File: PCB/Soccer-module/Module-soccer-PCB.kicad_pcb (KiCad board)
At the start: 2 copper layers, 60 x 60 mm, 6 parts, among them J2 Conn_01x06, J4 Conn_01x02, J5 Conn_01x02, J6 Conn_01x02, U1 TB6612

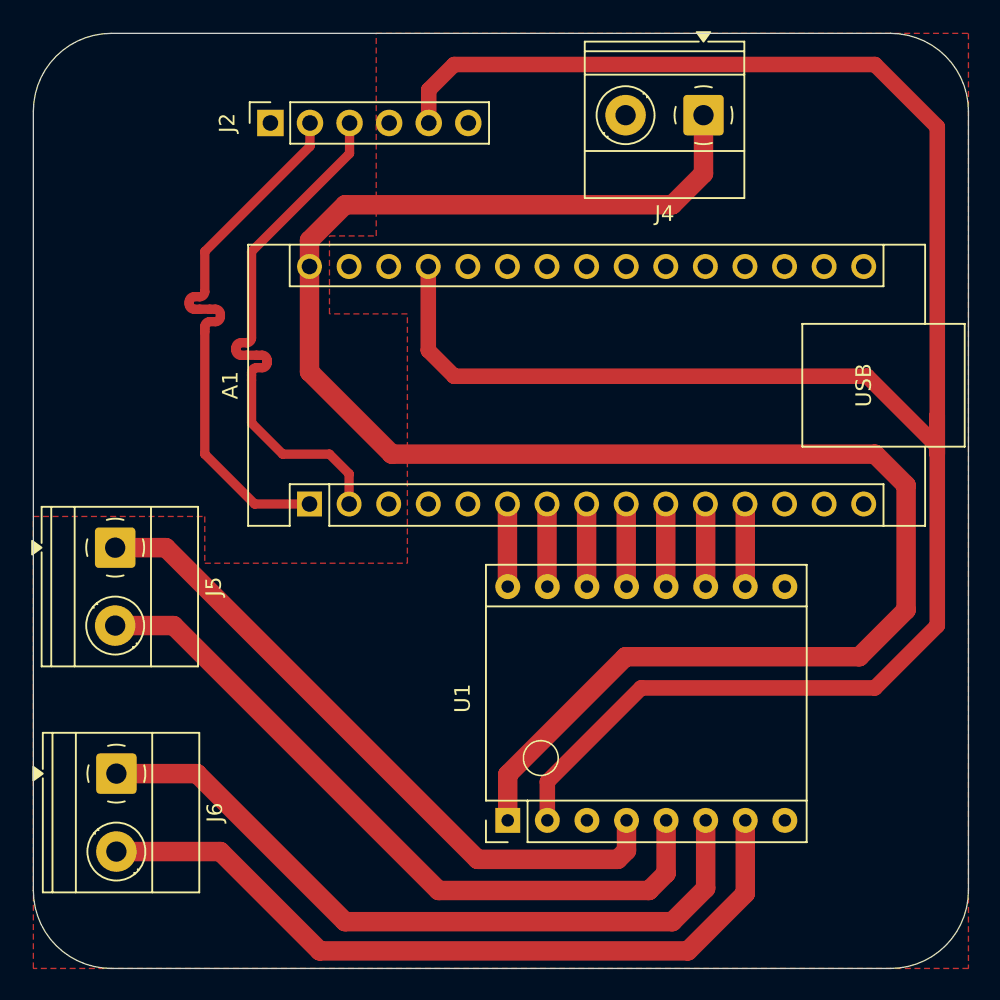
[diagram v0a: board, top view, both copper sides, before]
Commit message: Nuevos modelos del esquematico
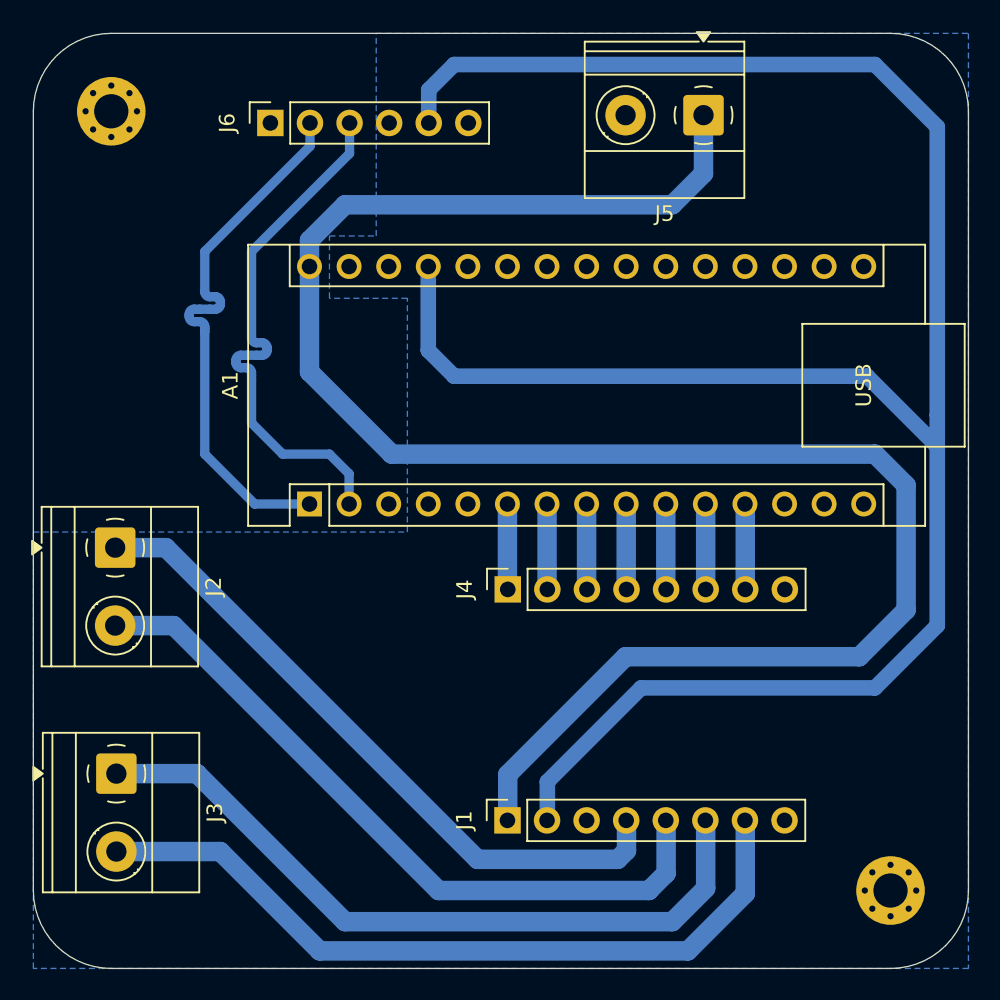
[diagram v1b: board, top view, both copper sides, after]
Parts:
- removed U1: TB6612, Footprints-soccer:TB6612_17.8x15
- added J1: Conn_01x08, Connector_PinSocket_2.54mm:PinSocket_1x08_P2.54mm_Vertical, F.Cu at (180.4, 100.5)
- added J4: Conn_01x08, Connector_PinSocket_2.54mm:PinSocket_1x08_P2.54mm_Vertical, F.Cu at (180.4, 85.7)
- added REF**: MountingHole_2.2mm_M2_Pad_Via, MountingHole:MountingHole_2.2mm_M2_Pad_Via, F.Cu at (205.0, 105.0)
- added REF**: MountingHole_2.2mm_M2_Pad_Via, MountingHole:MountingHole_2.2mm_M2_Pad_Via, F.Cu at (155.0, 55.0)
- renumbered J5 to J2, J6 to J3, J4 to J5, J2 to J6
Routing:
- net +5V: track 144.3 -> 141.3 mm
- added copper zone on B.Cu, net GND
- removed copper zone on F.Cu, net GND
